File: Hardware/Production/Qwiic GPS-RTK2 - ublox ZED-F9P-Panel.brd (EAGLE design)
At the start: 43.2 x 43.2 mm, 125 parts, among them J1 Radio, J13 U.FL, J3 PTH, U2 3.3V, U3 ZED-F9P

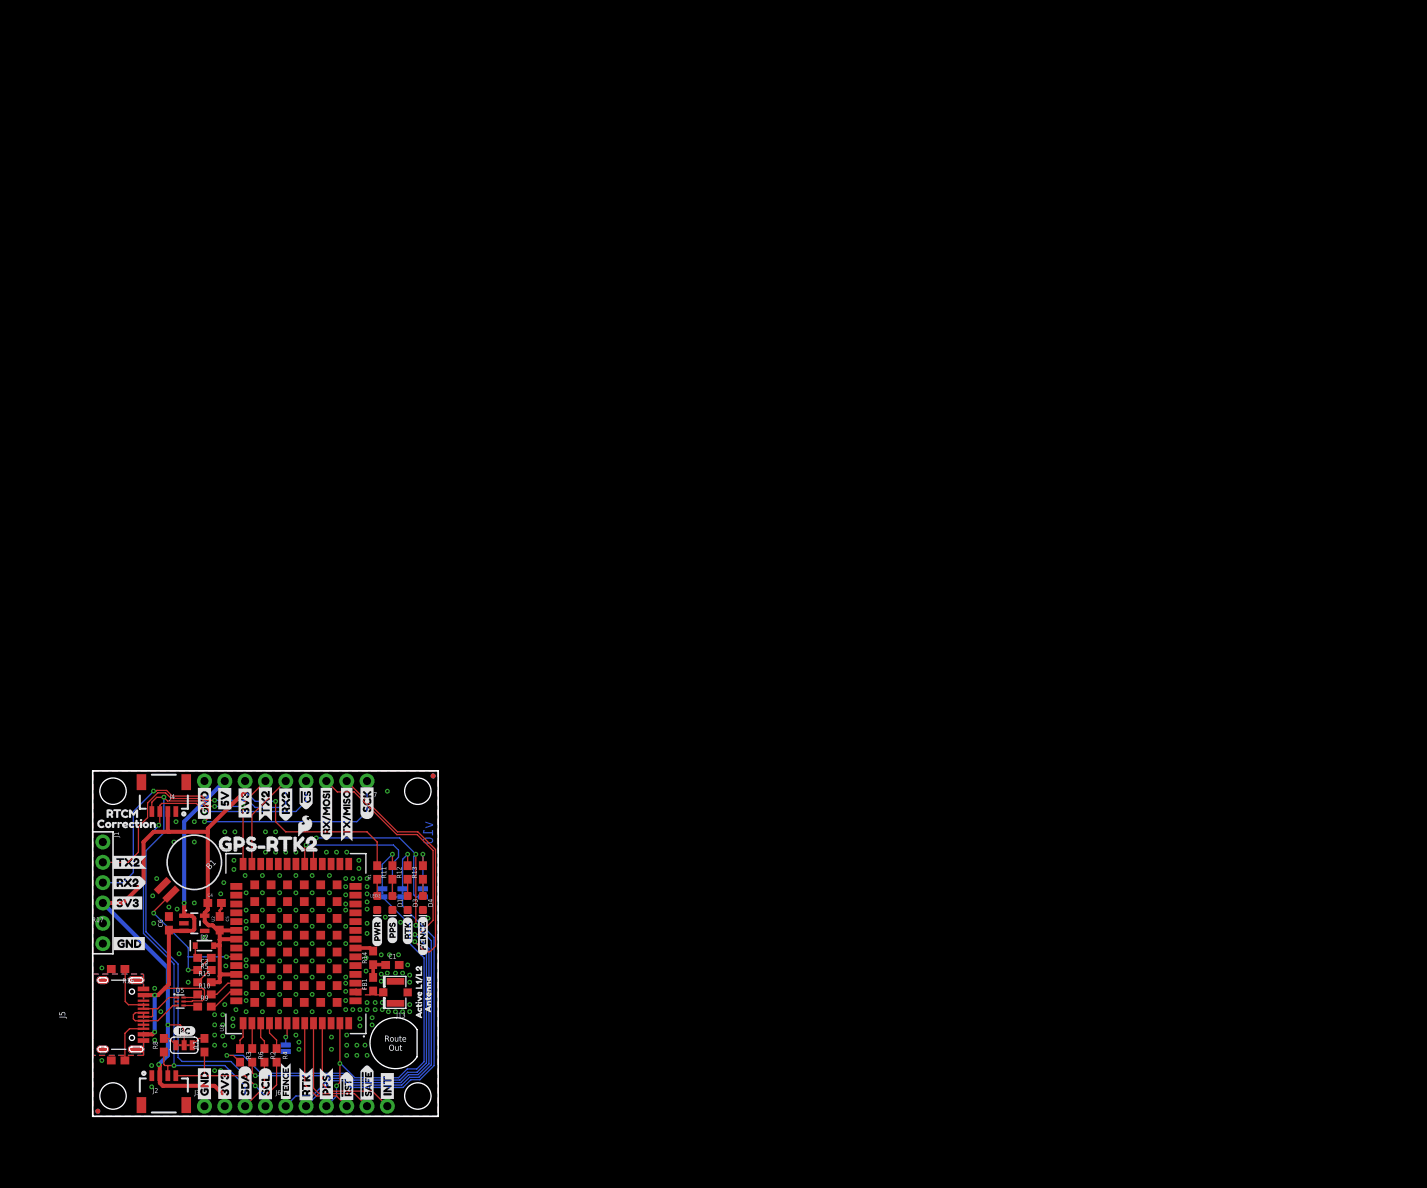
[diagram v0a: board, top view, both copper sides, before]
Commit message: v11 hardware: Added add' decoupling to USB VBUS, recomended induc to ant, more 33 ohm resistors.
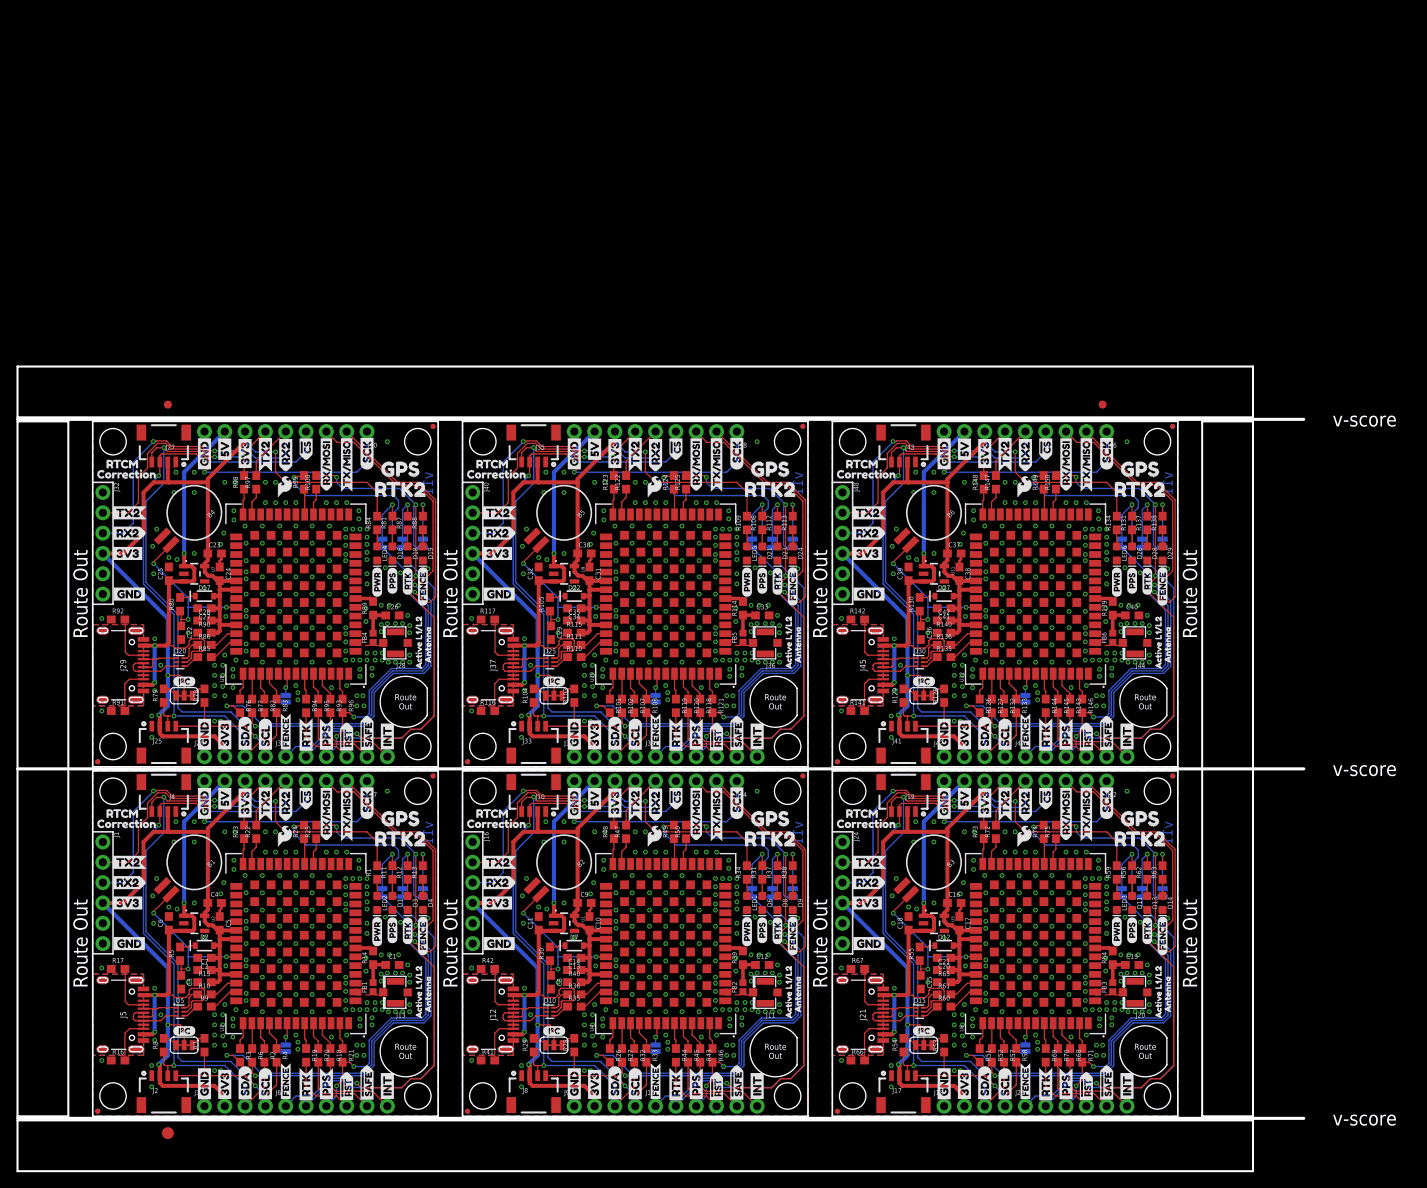
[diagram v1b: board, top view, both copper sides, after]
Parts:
- removed FRAME1: FRAME-LETTER, SparkFun-Aesthetics:CREATIVE_COMMONS
- added B2, B3, B4, B5, B6: 6.8MM_COIN_CELL, SparkFun-Batteries:BATTCON-6.8MM
- added C10, C14, C17, C21, C24, C28, C31, C35, C38, C42, C7: 0.1uF, SparkFun-Capacitors:0603
- added C11, C13, C15, C16, C18, C2, C20, C22, C23, C25, C27, C29, C30, C32, C34, C36, C37, C39, C41, C8, C9: 1.0uF, SparkFun-Capacitors:0603
- added C12, C19, C26, C33, C40: 47pF, SparkFun-Capacitors:0603
- added D10, D15, D20, D25, D30: PRTR5V0U2F, funbit:SOT886
- added D11, D16, D21, D26, D6: Yellow, SparkFun-LED:LED-0603
- added D12, D17, D22, D27, D7: 0.5A/40V/420mV, SparkFun-DiscreteSemi:SOD-323
- added D13, D18, D23, D28, D8: GREEN, SparkFun-LED:LED-0603
- added D14, D19, D24, D29, D9: BLUE, SparkFun-LED:LED-0603
- added E$1, E$2: (no value), SparkFun-Aesthetics:FIDUCIAL-1X2
- added E$3: (no value), SparkFun-Retired:FIDUCIAL-1.5X3
- added FB2, FB3, FB4, FB5, FB6: FERRITE_BEAD-120_OHM-0402, SparkFun-Coils:0402
- added J10, J17, J19, J25, J27, J33, J35, J41, J43, J8: (no value), SparkFun-Connectors:1X04_1MM_RA
- added J11, J20, J28, J36, J44: U.FL, SparkFun-Connectors:U.FL
- added J12, J21, J29, J37, J45: (no value), USB-C:USB-C-16P
- added J14, J22, J30, J38, J46: (no value), SparkFun-Connectors:1X09_NO_SILK
- added J15, J23, J31, J39, J47: (no value), SparkFun-Connectors:1X06_NO_SILK
- added J16, J24, J32, J40, J48: Radio, SparkFun-Connectors:1X06_NO_SILK
- added J18, J26, J34, J42, J9: PTH, SparkX:1X04_NO_SILK
- added JP10, JP24, JP38, JP52, JP66: (no value), SparkFun-Jumpers:SMT-JUMPER_3_2-NC_TRACE_SILK
- added JP11, JP17, JP18, JP25, JP32, JP33, JP39, JP46, JP47, JP53, JP59, JP60, JP67, JP74, JP75: (no value), SparkFun-Jumpers:SMT-JUMPER_2_NC_TRACE_SILK
- added JP12, JP13, JP22, JP23, JP26, JP27, JP36, JP37, JP40, JP42, JP50, JP51, JP54, JP55, JP64, JP65, JP68, JP69, JP8, JP9: FIDUCIALUFIDUCIAL, SparkFun:MICRO-FIDUCIAL
- added JP14, JP15, JP19, JP20, JP28, JP29, JP34, JP35, JP43, JP44, JP48, JP49, JP56, JP57, JP6, JP62, JP63, JP7, JP70, JP72: STAND-OFF, SparkFun:STAND-OFF
- added JP16, JP30, JP45, JP58, JP73: (no value), SparkFun-Jumpers:SMT-JUMPER_2_NO_SILK
- added LED1, LED3, LED4, LED5, LED6: RED, SparkFun-LED:LED-0603
- added LOGO10, LOGO12, LOGO4, LOGO6, LOGO8: SFE_LOGO_NAME_FLAME.1_INCH, SparkFun-Aesthetics:SFE_LOGO_NAME_FLAME_.1
- added LOGO11, LOGO3, LOGO5, LOGO7, LOGO9: OSHW-LOGOMINI, SparkFun-Aesthetics:OSHW-LOGO-MINI
- added R100, R101, R102, R107, R108, R118, R119, R120, R121, R122, R123, R124, R125, R126, R127, R132, R133, R143, R144, R145, R146, R147, R148, R149, R150, R18, R19, R20, R21, R22, R23, R24, R25, R26, R27, R32, R33, R43, R44, R45, R46, R47, R48, R49, R50, R51, R52, R57, R58, R68, R69, R70, R71, R72, R73, R74, R75, R76, R77, R82, R83, R93, R94, R95, R96, R97, R98, R99: 33, SparkFun-Resistors:0603
- added R103, R104, R128, R129, R28, R29, R53, R54, R78, R79: 2.2k, SparkFun-Resistors:0603
- added R105, R106, R109, R112, R113, R130, R131, R134, R137, R138, R30, R31, R34, R37, R38, R55, R56, R59, R62, R63, R80, R81, R84, R87, R88: 1k, SparkFun-Resistors:0603
- added R110, R111, R135, R136, R35, R36, R60, R61, R85, R86: 27, SparkFun-Resistors:0603
- added R114, R139, R39, R64, R89: 10, SparkFun-Resistors:0603
- added R115, R140, R40, R65, R90: 100k, SparkFun-Resistors:0603
- added R116, R117, R141, R142, R41, R42, R66, R67, R91, R92: 5.1k, SparkFun-Resistors:0603
- added U$100, U$145, U$146, U$168, U$169, U$214, U$215, U$237, U$238, U$283, U$284, U$306, U$307, U$352, U$353, U$375, U$376, U$76, U$77, U$99: (no value), Labels:GND-04
- added U$101, U$170, U$239, U$308, U$377: (no value), buzzard_labels (5):JP10
- added U$102, U$171, U$240, U$309, U$378: (no value), buzzard_labels (5):JP32
- added U$103, U$172, U$241, U$310, U$379: (no value), buzzard_labels (6):DSEL0
- added U$104, U$173, U$242, U$311, U$380: (no value), Labels:PWR-()-03
- added U$105, U$106, U$174, U$175, U$243, U$244, U$312, U$313, U$381, U$382: (no value), Labels:5V
- added U$107, U$108, U$176, U$177, U$245, U$246, U$314, U$315, U$383, U$384: (no value), Labels:CS#-<]
- added U$109, U$110, U$178, U$179, U$247, U$248, U$316, U$317, U$385, U$386: (no value), Labels:SCK-(]-04
- added U$111, U$180, U$249, U$318, U$387: (no value), SparkFun-Aesthetics:SFE_LOGO_FLAME_.1
- added U$112, U$124, U$181, U$193, U$250, U$262, U$319, U$331, U$388, U$400: (no value), buzzard_labels (36):RX#MOSI3
- added U$113, U$125, U$182, U$194, U$251, U$263, U$320, U$332, U$389, U$401: (no value), buzzard_labels (36):TX#MISO1
- added U$114, U$118, U$183, U$187, U$252, U$256, U$321, U$325, U$390, U$394: (no value), buzzard_labels (4):GND3
- added U$115, U$184, U$253, U$322, U$391: (no value), buzzard_labels (4):GPS#RTK28
- added U$116, U$117, U$143, U$144, U$166, U$167, U$185, U$186, U$212, U$213, U$235, U$236, U$254, U$255, U$281, U$282, U$304, U$305, U$323, U$324, U$350, U$351, U$373, U$374, U$392, U$393, U$74, U$75, U$97, U$98: (no value), Labels:3V3-04
- added U$119, U$123, U$188, U$192, U$257, U$261, U$326, U$330, U$395, U$399: (no value), buzzard_labels (4):CORRECTION0
- added U$120, U$122, U$189, U$191, U$258, U$260, U$327, U$329, U$396, U$398: (no value), buzzard_labels (4):RTCM5
- added U$121, U$190, U$259, U$328, U$397: (no value), buzzard_labels (4):ZED#F9P6
- added U$126, U$195, U$264, U$333, U$402: SMA-ANTENNA-THREADED, SparkFun-Hardware:SMA-THREADED
- added U$127, U$196, U$265, U$334, U$403: (no value), buzzard_labels (8):ACTIVE_L1#L21
- added U$128, U$197, U$266, U$335, U$404: (no value), buzzard_labels (8):ANTENNA2
- added U$129, U$134, U$136, U$198, U$203, U$205, U$267, U$272, U$274, U$336, U$341, U$343, U$405, U$410, U$412: (no value), buzzard_labels (10):RX20
- added U$130, U$199, U$268, U$337, U$406: (no value), buzzard_labels (10):RX22
- added U$131, U$133, U$135, U$200, U$202, U$204, U$269, U$271, U$273, U$338, U$340, U$342, U$407, U$409, U$411: (no value), buzzard_labels (10):TX21
- added U$132, U$201, U$270, U$339, U$408: (no value), buzzard_labels (10):TX23
- added U$137, U$206, U$275, U$344, U$413, U$59: (no value), buzzard_labels (4):GPS0
- added U$138, U$207, U$276, U$345, U$414, U$64: (no value), buzzard_labels (4):RTK21
- added U$139, U$141, U$208, U$210, U$277, U$279, U$346, U$348, U$72: (no value), Labels:SDA-[)
- added U$140, U$142, U$209, U$211, U$278, U$280, U$347, U$349, U$73: (no value), Labels:SCL-[)
- added U$147, U$216, U$285, U$354, U$78: (no value), Labels:I_SUPER2_C-()-03
- added U$148, U$149, U$217, U$218, U$286, U$287, U$355, U$356, U$79, U$80: (no value), buzzard_labels (5):INT8
- added U$150, U$219, U$288, U$357, U$81: (no value), buzzard_labels (5):U#BLOX3
- added U$151, U$220, U$289, U$358, U$82: (no value), Labels:QWIIC-LOGO-MEDIUM
- added U$152, U$153, U$221, U$222, U$290, U$291, U$359, U$360, U$83, U$84: (no value), buzzard_labels (7):#RST3
- added U$154, U$155, U$223, U$224, U$292, U$293, U$361, U$362, U$85, U$86: (no value), buzzard_labels (7):#SAFE1
- added U$156, U$157, U$225, U$226, U$294, U$295, U$363, U$364, U$87, U$88: (no value), buzzard_labels (7):PPS5
- added U$158, U$227, U$296, U$365, U$89: (no value), buzzard_labels (33):PPS0
- added U$159, U$228, U$297, U$366, U$90: (no value), buzzard_labels:FENCE2
- added U$160, U$229, U$298, U$367, U$91: (no value), buzzard_labels:JP20
- added U$161, U$230, U$299, U$368, U$92: (no value), buzzard_labels:RTK1
- added U$162, U$163, U$231, U$232, U$300, U$301, U$369, U$370, U$93, U$94: (no value), buzzard_labels (1):FENCE0
- added U$164, U$165, U$233, U$234, U$302, U$303, U$371, U$372, U$95, U$96: (no value), buzzard_labels (1):RTK1
- added U1, U11, U5, U7, U9: 3.3V, SparkFun-IC-Power:SOT23-5
- added U10, U12, U4, U6, U8: ZED-F9P, ZED-F9P:ZED-F9P
- FB1: value 30Ω/1.8A -> FERRITE_BEAD-120_OHM-0402; device SparkFun-Coils:0603 -> SparkFun-Coils:0402
- U$2: value SPECIAL_INSTRUCTIONS-ORDERING -> (none); device SparkFun-Aesthetics:ORDERING_INSTRUCTIONS -> Labels:SDA-[)
- U$47: device buzzard_labels (4):GPS#RTK29 -> Labels:SCL-[)
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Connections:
- new net !RESET1: J15.4, R44.2
- new net !RESET2: J23.4, R69.2
- new net !RESET3: J31.4, R94.2
- new net !RESET4: J39.4, R119.2
- new net !RESET5: J47.4, R144.2
- new net !SAFE1: J15.5, R45.2
- new net !SAFE2: J23.5, R70.2
- new net !SAFE3: J31.5, R95.2
- new net !SAFE4: J39.5, R120.2
- new net !SAFE5: J47.5, R145.2
- new net 3.3V1: C10.2, C13.1, C14.2, C9.1, D7.A, J10.2, J14.7, J16.4, J8.2, J9.2, JP10.2, R34.2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
- new net 3.3V2: C16.1, C17.2, C20.1, C21.2, D12.A, J17.2, J18.2, J19.2, J22.7, J24.4, JP24.2, R59.2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
- new net 3.3V3: C23.1, C24.2, C27.1, C28.2, D17.A, J25.2, J26.2, J27.2, J30.7, J32.4, JP38.2, R84.2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
- new net 3.3V4: C30.1, C31.2, C34.1, C35.2, D22.A, J33.2, J34.2, J35.2, J38.7, J40.4, JP52.2, R109.2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
- new net 3.3V5: C37.1, C38.2, C41.1, C42.2, D27.A, J41.2, J42.2, J43.2, J46.7, J48.4, JP66.2, R134.2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
- new net 5V1: C11.1, D10.5, J12.VBUS1, J12.VBUS2, J14.8, U1.1, U1.3
- new net 5V2: C18.1, D15.5, J21.VBUS1, J21.VBUS2, J22.8, U5.1, U5.3
- new net 5V3: C25.1, D20.5, J29.VBUS1, J29.VBUS2, J30.8, U7.1, U7.3
- new net 5V4: C32.1, D25.5, J37.VBUS1, J37.VBUS2, J38.8, U9.1, U9.3
- new net 5V5: C39.1, D30.5, J45.VBUS1, J45.VBUS2, J46.8, U11.1, U11.3
- new net ANT_VCC1: C12.1, FB2.2, R39.1
- new net ANT_VCC2: C19.1, FB3.2, R64.1
- new net ANT_VCC3: C26.1, FB4.2, R89.1
- new net ANT_VCC4: C33.1, FB5.2, R114.1
- new net ANT_VCC5: C40.1, FB6.2, R139.1
- new net BACKUP1: B2.+, C8.1, R30.1, U4.36
- new net BACKUP2: B3.+, C15.1, R55.1, U6.36
- new net BACKUP3: B4.+, C22.1, R80.1, U8.36
- new net BACKUP4: B5.+, C29.1, R105.1, U10.36
- new net BACKUP5: B6.+, C36.1, R130.1, U12.36
- new net CC10: J37.B5, R116.2
- new net CC11: J45.A5, R142.2
- new net CC12: J45.B5, R141.2
- new net CC3: J12.A5, R42.2
- new net CC4: J12.B5, R41.2
- new net CC5: J21.A5, R67.2
- new net CC6: J21.B5, R66.2
- new net CC7: J29.A5, R92.2
- new net CC8: J29.B5, R91.2
- new net CC9: J37.A5, R117.2
- new net D+1: D10.4, R35.1
- new net D+2: D15.4, R60.1
- new net D+3: D20.4, R85.1
- new net D+4: D25.4, R110.1
- new net D+5: D30.4, R135.1
- new net D-1: D10.6, R36.1
- new net D-2: D15.6, R61.1
- new net D-3: D20.6, R86.1
- new net D-4: D25.6, R111.1
- new net D-5: D30.6, R136.1
- new net D_SEL1: JP16.2, U4.47
- new net D_SEL2: JP30.2, U6.47
- new net D_SEL3: JP45.2, U8.47
- new net D_SEL4: JP58.2, U10.47
- new net D_SEL5: JP73.2, U12.47
- new net FENCE_STAT1: J15.1, JP18.2, R50.2
- new net FENCE_STAT2: J23.1, JP33.2, R75.2
- new net FENCE_STAT3: J31.1, JP47.2, R100.2
- new net FENCE_STAT4: J39.1, JP60.2, R125.2
- new net FENCE_STAT5: J47.1, JP75.2, R150.2
- new net GND1: B2.-, C10.1, C11.2, C12.2, C13.2, C14.1, C8.2, C9.2, D10.2, D6.C, D8.C, D9.C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
- new net GND2: B3.-, C15.2, C16.2, C17.1, C18.2, C19.2, C20.2, C21.1, D11.C, D13.C, D14.C, D15.2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
- new net GND3: B4.-, C22.2, C23.2, C24.1, C25.2, C26.2, C27.2, C28.1, D16.C, D18.C, D19.C, D20.2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
- new net GND4: B5.-, C29.2, C30.2, C31.1, C32.2, C33.2, C34.2, C35.1, D21.C, D23.C, D24.C, D25.2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
- new net GND5: B6.-, C36.2, C37.2, C38.1, C39.2, C40.2, C41.2, C42.1, D26.C, D28.C, D29.C, D30.2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
- new net GPS_ANT2: FB2.1, J11.FEED, U4.2
- new net GPS_ANT3: FB3.1, J20.FEED, U6.2
- new net GPS_ANT4: FB4.1, J28.FEED, U8.2
- new net GPS_ANT5: FB5.1, J36.FEED, U10.2
- new net GPS_ANT6: FB6.1, J44.FEED, U12.2
- new net INT1: J15.6, R43.2
- new net INT2: J23.6, R68.2
- new net INT3: J31.6, R93.2
- new net INT4: J39.6, R118.2
- new net INT5: J47.6, R143.2
- new net N$100: R125.1, U10.19
- new net N$101: JP66.1, R129.2
- new net N$102: JP66.3, R128.2
- new net N$103: D26.A, R131.1
- new net N$104: JP67.1, R131.2
- new net N$105: D27.C, R130.2
- new net N$106: LED6.A, R134.1
- new net N$107: R135.2, U12.40
- new net N$108: R136.2, U12.39
- new net N$109: D28.A, R137.1
- new net N$110: JP74.1, R137.2
- new net N$111: D29.A, R138.1
- new net N$112: JP75.1, R138.2
- new net N$113: R139.2, U12.7
- new net N$114: R147.1, U12.26
- new net N$115: R143.1, U12.51
- new net N$116: R144.1, U12.49
- new net N$117: R146.1, U12.53
- new net N$118: R145.1, U12.50
- new net N$119: R149.1, U12.20
- new net N$120: R150.1, U12.19
- new net N$14: R22.1, U3.26
- new net N$15: R18.1, U3.51
- new net N$16: R19.1, U3.49
- new net N$17: R21.1, U3.53
- new net N$18: R20.1, U3.50
- new net N$19: R24.1, U3.20
- new net N$20: R25.1, U3.19
- new net N$21: JP10.1, R29.2
- new net N$22: JP10.3, R28.2
- new net N$23: D6.A, R31.1
- new net N$24: JP11.1, R31.2
- new net N$25: D7.C, R30.2
- new net N$26: LED1.A, R34.1
- new net N$27: R35.2, U4.40
- new net N$28: R36.2, U4.39
- new net N$29: D8.A, R37.1
- new net N$30: JP17.1, R37.2
- new net N$31: D9.A, R38.1
- new net N$32: JP18.1, R38.2
- new net N$33: R39.2, U4.7
- new net N$34: R47.1, U4.26
- new net N$35: R43.1, U4.51
- new net N$36: R44.1, U4.49
- new net N$37: R46.1, U4.53
- new net N$38: R45.1, U4.50
- new net N$39: R49.1, U4.20
- new net N$40: R50.1, U4.19
- new net N$41: JP24.1, R54.2
- new net N$42: JP24.3, R53.2
- new net N$43: D11.A, R56.1
- new net N$44: JP25.1, R56.2
- new net N$45: D12.C, R55.2
- new net N$46: LED3.A, R59.1
- new net N$47: R60.2, U6.40
- new net N$48: R61.2, U6.39
- new net N$49: D13.A, R62.1
- new net N$50: JP32.1, R62.2
- new net N$51: D14.A, R63.1
- new net N$52: JP33.1, R63.2
- new net N$53: R64.2, U6.7
- new net N$54: R72.1, U6.26
- new net N$55: R68.1, U6.51
- new net N$56: R69.1, U6.49
- new net N$57: R71.1, U6.53
- new net N$58: R70.1, U6.50
- new net N$59: R74.1, U6.20
- new net N$60: R75.1, U6.19
- new net N$61: JP38.1, R79.2
- new net N$62: JP38.3, R78.2
- new net N$63: D16.A, R81.1
- new net N$64: JP39.1, R81.2
- new net N$65: D17.C, R80.2
- new net N$66: LED4.A, R84.1
- new net N$67: R85.2, U8.40
- new net N$68: R86.2, U8.39
- new net N$69: D18.A, R87.1
- new net N$70: JP46.1, R87.2
- new net N$71: D19.A, R88.1
- new net N$72: JP47.1, R88.2
- new net N$73: R89.2, U8.7
- new net N$74: R97.1, U8.26
- new net N$75: R93.1, U8.51
- new net N$76: R94.1, U8.49
- new net N$77: R96.1, U8.53
- new net N$78: R95.1, U8.50
- new net N$79: R99.1, U8.20
- new net N$80: R100.1, U8.19
- new net N$81: JP52.1, R104.2
- new net N$82: JP52.3, R103.2
- new net N$83: D21.A, R106.1
- new net N$84: JP53.1, R106.2
- new net N$85: D22.C, R105.2
- new net N$86: LED5.A, R109.1
- new net N$87: R110.2, U10.40
- new net N$88: R111.2, U10.39
- new net N$89: D23.A, R112.1
- new net N$90: JP59.1, R112.2
- new net N$91: D24.A, R113.1
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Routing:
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- added copper zone on layer 1, net GND1
- added copper zone on layer 16, net GND1
- added copper zone on layer 1, net GND2
- added copper zone on layer 16, net GND2
- added copper zone on layer 1, net GND3
- added copper zone on layer 16, net GND3
- added copper zone on layer 1, net GND4
- added copper zone on layer 16, net GND4
- added copper zone on layer 1, net GND5
- added copper zone on layer 16, net GND5
- added copper zone on layer 1, net GPS_ANT2
- added copper zone on layer 1, net GPS_ANT3
- added copper zone on layer 1, net GPS_ANT4
- added copper zone on layer 1, net GPS_ANT5
- added copper zone on layer 1, net GPS_ANT6
- added copper zone on layer 1, net SHLD1
- added copper zone on layer 16, net SHLD1
- added copper zone on layer 1, net SHLD2
- added copper zone on layer 16, net SHLD2
- added copper zone on layer 1, net SHLD3
- added copper zone on layer 16, net SHLD3
- added copper zone on layer 1, net SHLD4
- added copper zone on layer 16, net SHLD4
- added copper zone on layer 1, net SHLD5
- added copper zone on layer 16, net SHLD5
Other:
- board size 43.2 x 43.2 mm -> 160.8 x 100.6 mm
- board text added: "Route Out"
- board text added: "v-score"
- board text added: "v11"
- board text removed: "Board thickness is 0.8mm"
- board text removed: "Measurements in inches"
- board text removed: "No clean process"
- board text removed: "v10"

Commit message: Adding SMA connector to Antenna and SMA
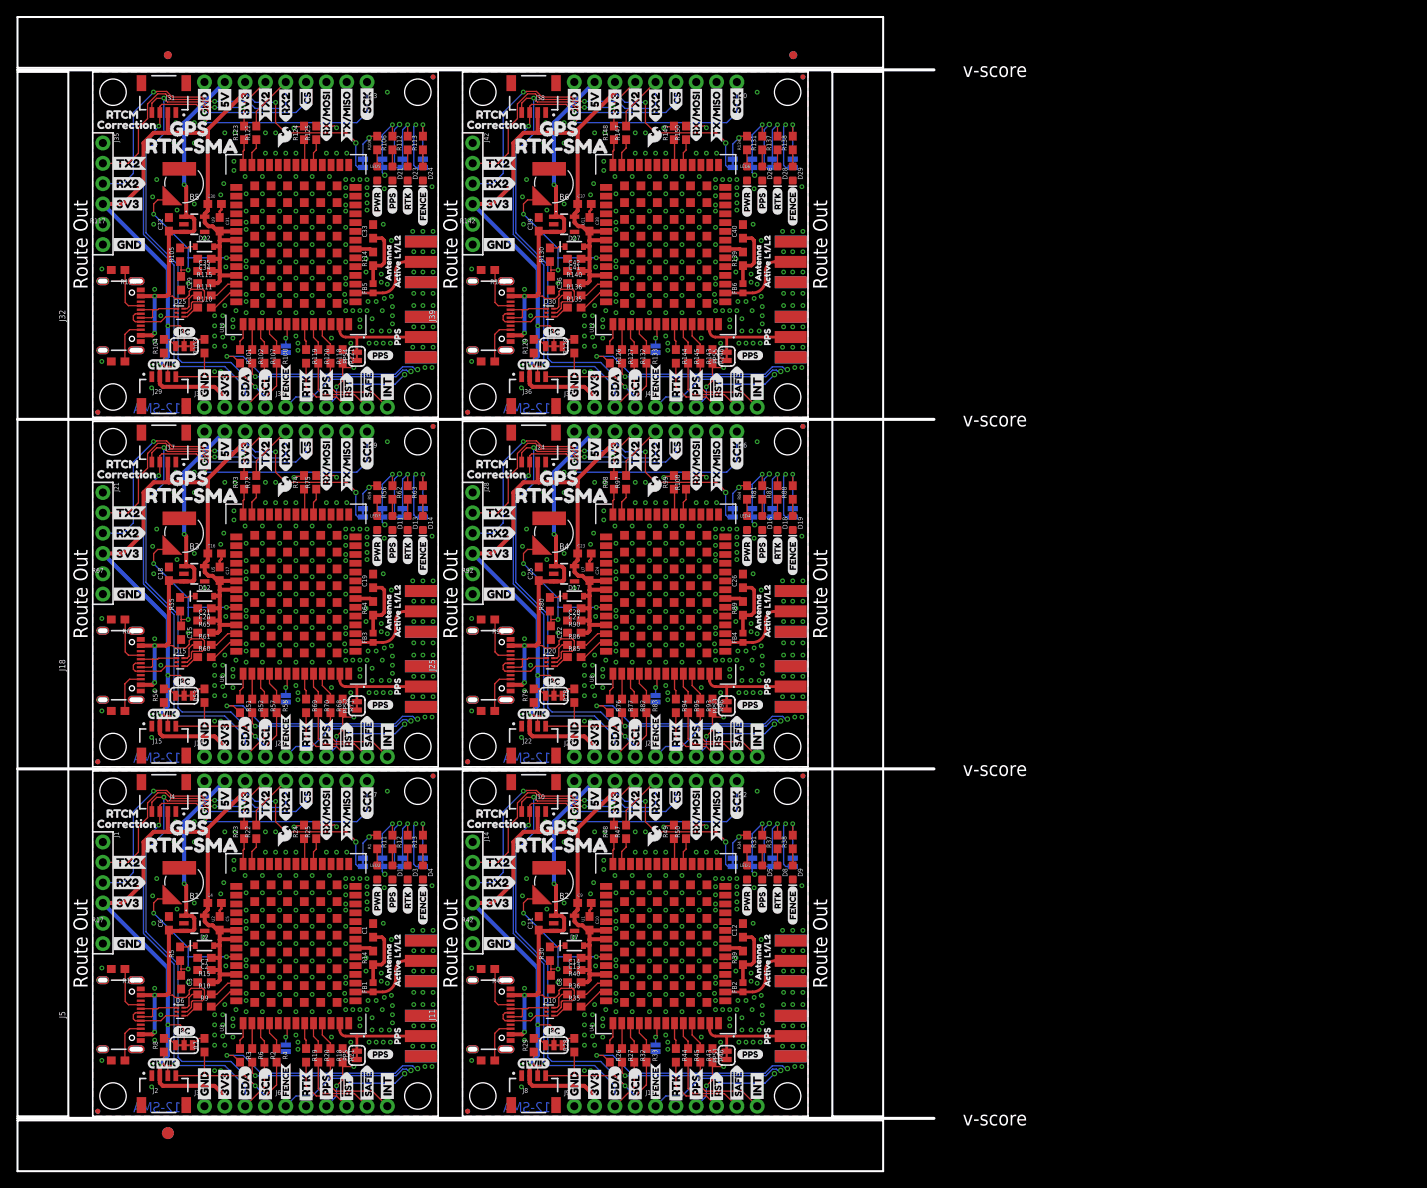
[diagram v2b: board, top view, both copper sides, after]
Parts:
- removed J43: (no value), SparkFun-Connectors:1X04_1MM_RA
- removed J44: U.FL, SparkFun-Connectors:U.FL
- removed J45: (no value), USB-C:USB-C-16P
- removed J46: (no value), SparkFun-Connectors:1X09_NO_SILK
- removed J47: (no value), SparkFun-Connectors:1X06_NO_SILK
- removed J48: Radio, SparkFun-Connectors:1X06_NO_SILK
- removed JP50, JP51, JP54, JP55, JP64, JP65, JP68, JP69: FIDUCIALUFIDUCIAL, SparkFun:MICRO-FIDUCIAL
- removed JP52, JP66: (no value), SparkFun-Jumpers:SMT-JUMPER_3_2-NC_TRACE_SILK
- removed JP53, JP59, JP60, JP67, JP74, JP75: (no value), SparkFun-Jumpers:SMT-JUMPER_2_NC_TRACE_SILK
- removed JP56, JP57, JP62, JP63, JP70, JP72: STAND-OFF, SparkFun:STAND-OFF
- removed JP73: (no value), SparkFun-Jumpers:SMT-JUMPER_2_NO_SILK
- added E$4: (no value), SparkFun-Aesthetics:FIDUCIAL-1X2
- added E$5, E$6: (no value), SparkFun-Retired:FIDUCIAL-1.5X3
- added E1, E10, E11, E12, E2, E3, E4, E5, E6, E7, E8, E9: SMA, SparkFun-RF:SMA-EDGE
- added FENCE, FENCE1, FENCE2, FENCE3, FENCE4, FENCE5, PPS, PPS1, PPS2, PPS3, PPS4, PPS5, PPS_LED, PPS_LED1, PPS_LED2, PPS_LED3, PPS_LED4, PPS_LED5, PWR, PWR1, PWR2, PWR3, PWR4, PWR5, RTK, RTK1, RTK2, RTK3, RTK4, RTK5: (no value), SparkFun-Jumpers:SMT-JUMPER_2_NC_TRACE_SILK
- added SPI, SPI1, SPI2, SPI4, SPI5: (no value), SparkFun-Jumpers:SMT-JUMPER_2_NO_SILK
- added U$415: (no value), buzzard_labels (36):RX#MOSI3
- added U$416: (no value), buzzard_labels (36):TX#MISO1
- added U$417: (no value), buzzard_labels (8):ACTIVE_L1#L21
- added U$418, U$437: (no value), buzzard_labels (8):ANTENNA2
- added U$419, U$424, U$426: (no value), buzzard_labels (10):RX20
- added U$420: (no value), buzzard_labels (10):RX22
- added U$421, U$423, U$425: (no value), buzzard_labels (10):TX21
- added U$422: (no value), buzzard_labels (10):TX23
- added U$427: (no value), buzzard_labels (4):GPS0
- added U$428: (no value), SparkFun-Aesthetics:QWIIC_4MM
- added U$429, U$436: (no value), buzzard_labels (2):PPS1
- added U$430: (no value), Labels:PWR-()-03
- added U$431, U$434: (no value), buzzard_labels (33):PPS0
- added U$432: (no value), buzzard_labels:RTK1
- added U$433: (no value), buzzard_labels:FENCE2
- added U$435: (no value), buzzard_labels (3):RTK#SMA4
- added U$438: (no value), buzzard_labels (4):GPS#RTK#SMA5
- B1, B2, B3, B4, B5, B6: device SparkFun-Batteries:BATTCON-6.8MM -> SparkFun-Batteries:ML414H_IV01E
- D10, D15, D20, D25, D30: device funbit:SOT886 -> SparkFun-IC-Power:SOT886
- D5: value PRTR5V0U2F -> Yellow; device funbit:SOT886 -> SparkFun-LED:LED-0603
- D6: value Yellow -> PRTR5V0U2F; device SparkFun-LED:LED-0603 -> SparkFun-IC-Power:SOT886
- E$3: device SparkFun-Retired:FIDUCIAL-1.5X3 -> SparkFun-Aesthetics:FIDUCIAL-1X2
- FB1, FB2, FB3, FB4, FB5, FB6: value FERRITE_BEAD-120_OHM-0402 -> 120_OHM
- J10, J17, J2, J4, J8: value (none) -> Qwiic Right Angle; device SparkFun-Connectors:1X04_1MM_RA -> SparkFun-Connectors:JST04_1MM_RA
- J11: value U.FL -> (none); device SparkFun-Connectors:U.FL -> SparkFun-Connectors:USB-C-16P-2LAYER-PADS
- J12: device USB-C:USB-C-16P -> SparkFun-Connectors:1X09_NO_SILK
- J13, J20: value U.FL -> (none); device SparkFun-Connectors:U.FL -> SparkFun-Connectors:1X06_NO_SILK
- J14: value (none) -> Radio; device SparkFun-Connectors:1X09_NO_SILK -> SparkFun-Connectors:1X06_NO_SILK
- J15, J31: value (none) -> Qwiic Right Angle; device SparkFun-Connectors:1X06_NO_SILK -> SparkFun-Connectors:JST04_1MM_RA
- J16: value Radio -> PTH; device SparkFun-Connectors:1X06_NO_SILK -> SparkX:1X04_NO_SILK
- J18: value PTH -> (none); device SparkX:1X04_NO_SILK -> SparkFun-Connectors:USB-C-16P-2LAYER-PADS
- J19, J33: device SparkFun-Connectors:1X04_1MM_RA -> SparkFun-Connectors:1X09_NO_SILK
- J21: value (none) -> Radio; device USB-C:USB-C-16P -> SparkFun-Connectors:1X06_NO_SILK
- J22, J38: value (none) -> Qwiic Right Angle; device SparkFun-Connectors:1X09_NO_SILK -> SparkFun-Connectors:JST04_1MM_RA
- J23: value (none) -> PTH; device SparkFun-Connectors:1X06_NO_SILK -> SparkX:1X04_NO_SILK
- J24: value Radio -> Qwiic Right Angle; device SparkFun-Connectors:1X06_NO_SILK -> SparkFun-Connectors:JST04_1MM_RA
- J25: device SparkFun-Connectors:1X04_1MM_RA -> SparkFun-Connectors:USB-C-16P-2LAYER-PADS
- J26: value PTH -> (none); device SparkX:1X04_NO_SILK -> SparkFun-Connectors:1X09_NO_SILK
- J27, J41: device SparkFun-Connectors:1X04_1MM_RA -> SparkFun-Connectors:1X06_NO_SILK
- J28: value U.FL -> Radio; device SparkFun-Connectors:U.FL -> SparkFun-Connectors:1X06_NO_SILK
- J29: value (none) -> Qwiic Right Angle; device USB-C:USB-C-16P -> SparkFun-Connectors:JST04_1MM_RA
- J30: value (none) -> PTH; device SparkFun-Connectors:1X09_NO_SILK -> SparkX:1X04_NO_SILK
- J32: value Radio -> (none); device SparkFun-Connectors:1X06_NO_SILK -> SparkFun-Connectors:USB-C-16P-2LAYER-PADS
- J34: value PTH -> (none); device SparkX:1X04_NO_SILK -> SparkFun-Connectors:1X06_NO_SILK
- J35: value (none) -> Radio; device SparkFun-Connectors:1X04_1MM_RA -> SparkFun-Connectors:1X06_NO_SILK
- J36: value U.FL -> Qwiic Right Angle; device SparkFun-Connectors:U.FL -> SparkFun-Connectors:JST04_1MM_RA
- J37: value (none) -> PTH; device USB-C:USB-C-16P -> SparkX:1X04_NO_SILK
- J39: device SparkFun-Connectors:1X06_NO_SILK -> SparkFun-Connectors:USB-C-16P-2LAYER-PADS
- J40: value Radio -> (none); device SparkFun-Connectors:1X06_NO_SILK -> SparkFun-Connectors:1X09_NO_SILK
- J42: value PTH -> Radio; device SparkX:1X04_NO_SILK -> SparkFun-Connectors:1X06_NO_SILK
- J5: device USB-C:USB-C-16P -> SparkFun-Connectors:USB-C-16P-2LAYER-PADS
- JP1, JP11, JP18, JP2, JP32, JP39: value (none) -> STAND-OFF; device SparkFun-Jumpers:SMT-JUMPER_2_NC_TRACE_SILK -> SparkFun:STAND-OFF
- JP10, JP38: value (none) -> STAND-OFF; device SparkFun-Jumpers:SMT-JUMPER_3_2-NC_TRACE_SILK -> SparkFun:STAND-OFF
- JP12, JP22, JP40, JP42, JP9: value FIDUCIALUFIDUCIAL -> STAND-OFF; device SparkFun:MICRO-FIDUCIAL -> SparkFun:STAND-OFF
- JP14, JP34, JP43, JP44, JP7: value STAND-OFF -> FIDUCIALUFIDUCIAL; device SparkFun:STAND-OFF -> SparkFun:MICRO-FIDUCIAL
- JP15, JP35, JP6: value STAND-OFF -> (none); device SparkFun:STAND-OFF -> SparkFun-Jumpers:SMT-JUMPER_3_2-NC_TRACE_SILK
- JP16, JP4: value (none) -> FIDUCIALUFIDUCIAL; device SparkFun-Jumpers:SMT-JUMPER_2_NO_SILK -> SparkFun:MICRO-FIDUCIAL
- JP17, JP3, JP33, JP46, JP47: value (none) -> FIDUCIALUFIDUCIAL; device SparkFun-Jumpers:SMT-JUMPER_2_NC_TRACE_SILK -> SparkFun:MICRO-FIDUCIAL
- JP24: value (none) -> FIDUCIALUFIDUCIAL; device SparkFun-Jumpers:SMT-JUMPER_3_2-NC_TRACE_SILK -> SparkFun:MICRO-FIDUCIAL
- JP25: device SparkFun-Jumpers:SMT-JUMPER_2_NC_TRACE_SILK -> SparkFun-Jumpers:SMT-JUMPER_3_2-NC_TRACE_SILK
- JP30: value (none) -> STAND-OFF; device SparkFun-Jumpers:SMT-JUMPER_2_NO_SILK -> SparkFun:STAND-OFF
- JP45: device SparkFun-Jumpers:SMT-JUMPER_2_NO_SILK -> SparkFun-Jumpers:SMT-JUMPER_3_2-NC_TRACE_SILK
- U$100, U$99: device Labels:GND-04 -> Labels:3V3-04
- U$101: device buzzard_labels (5):JP10 -> Labels:GND-04
- U$102: device buzzard_labels (5):JP32 -> Labels:GND-04
- U$115, U$391: device buzzard_labels (4):GPS#RTK28 -> Labels:3V3-04
- U$117: device Labels:3V3-04 -> buzzard_labels (4):GND3
- U$118: device buzzard_labels (4):GND3 -> buzzard_labels (4):CORRECTION0
- U$119, U$192: device buzzard_labels (4):CORRECTION0 -> buzzard_labels (4):RTCM5
- U$12: device buzzard_labels:JP20 -> Labels:PWR-()-03
- U$120: device buzzard_labels (4):RTCM5 -> buzzard_labels (4):ZED#F9P6
- U$121: device buzzard_labels (4):ZED#F9P6 -> buzzard_labels (4):RTCM5
- U$122, U$191: device buzzard_labels (4):RTCM5 -> buzzard_labels (4):CORRECTION0
- U$123: device buzzard_labels (4):CORRECTION0 -> buzzard_labels (36):RX#MOSI3
- U$124: device buzzard_labels (36):RX#MOSI3 -> buzzard_labels (36):TX#MISO1
- U$125: device buzzard_labels (36):TX#MISO1 -> buzzard_labels (8):ACTIVE_L1#L21
- U$126: value SMA-ANTENNA-THREADED -> (none); device SparkFun-Hardware:SMA-THREADED -> buzzard_labels (8):ANTENNA2
- U$127: device buzzard_labels (8):ACTIVE_L1#L21 -> buzzard_labels (10):RX20
- U$128: device buzzard_labels (8):ANTENNA2 -> buzzard_labels (10):RX22
- U$129: device buzzard_labels (10):RX20 -> buzzard_labels (10):TX21
- U$130: device buzzard_labels (10):RX22 -> buzzard_labels (10):TX23
- U$132: device buzzard_labels (10):TX23 -> buzzard_labels (10):RX20
- U$135: device buzzard_labels (10):TX21 -> buzzard_labels (4):GPS0
- U$136: device buzzard_labels (10):RX20 -> SparkFun-Aesthetics:QWIIC_4MM
- U$137: device buzzard_labels (4):GPS0 -> buzzard_labels (2):PPS1
- U$138: device buzzard_labels (4):RTK21 -> Labels:PWR-()-03
- U$139, U$72: device Labels:SDA-[) -> buzzard_labels (33):PPS0
- U$140: device Labels:SCL-[) -> buzzard_labels:RTK1
- U$141: device Labels:SDA-[) -> buzzard_labels:FENCE2
- U$142: device Labels:SCL-[) -> buzzard_labels (33):PPS0
- U$143: device Labels:3V3-04 -> buzzard_labels (3):RTK#SMA4
- U$144, U$74: device Labels:3V3-04 -> buzzard_labels (2):PPS1
- U$145: device Labels:GND-04 -> buzzard_labels (8):ANTENNA2
- U$146, U$76: device Labels:GND-04 -> buzzard_labels (4):GPS#RTK#SMA5
- U$147: device Labels:I_SUPER2_C-()-03 -> Labels:SDA-[)
- U$148: device buzzard_labels (5):INT8 -> Labels:SCL-[)
- U$149: device buzzard_labels (5):INT8 -> Labels:SDA-[)
- U$150: device buzzard_labels (5):U#BLOX3 -> Labels:SCL-[)
- U$151: device Labels:QWIIC-LOGO-MEDIUM -> Labels:3V3-04
- U$152: device buzzard_labels (7):#RST3 -> Labels:3V3-04
- U$153: device buzzard_labels (7):#RST3 -> Labels:GND-04
- U$154: device buzzard_labels (7):#SAFE1 -> Labels:GND-04
- U$155: device buzzard_labels (7):#SAFE1 -> Labels:I_SUPER2_C-()-03
- U$156, U$157: device buzzard_labels (7):PPS5 -> buzzard_labels (5):INT8
- U$158: device buzzard_labels (33):PPS0 -> buzzard_labels (5):U#BLOX3
- U$159: device buzzard_labels:FENCE2 -> buzzard_labels (7):#RST3
- U$160: device buzzard_labels:JP20 -> buzzard_labels (7):#RST3
- U$161: device buzzard_labels:RTK1 -> buzzard_labels (7):#SAFE1
- U$162: device buzzard_labels (1):FENCE0 -> buzzard_labels (7):#SAFE1
- U$163: device buzzard_labels (1):FENCE0 -> buzzard_labels (7):PPS5
- U$164: device buzzard_labels (1):RTK1 -> buzzard_labels (7):PPS5
- U$165: device buzzard_labels (1):RTK1 -> buzzard_labels (33):PPS0
- U$166: device Labels:3V3-04 -> buzzard_labels:FENCE2
- U$167, U$213: device Labels:3V3-04 -> buzzard_labels:RTK1
- U$168, U$169: device Labels:GND-04 -> buzzard_labels (1):FENCE0
- U$170: device buzzard_labels (5):JP10 -> buzzard_labels (1):RTK1
- U$171: device buzzard_labels (5):JP32 -> buzzard_labels (1):RTK1
- U$172: device buzzard_labels (6):DSEL0 -> Labels:3V3-04
- U$173: device Labels:PWR-()-03 -> Labels:3V3-04
- U$174, U$175: device Labels:5V -> Labels:GND-04
- U$176: device Labels:CS#-<] -> buzzard_labels (6):DSEL0
- U$177: device Labels:CS#-<] -> Labels:PWR-()-03
- U$178, U$179: device Labels:SCK-(]-04 -> Labels:5V
- U$180: device SparkFun-Aesthetics:SFE_LOGO_FLAME_.1 -> Labels:CS#-<]
- U$181, U$400: device buzzard_labels (36):RX#MOSI3 -> Labels:CS#-<]
- U$182, U$401: device buzzard_labels (36):TX#MISO1 -> Labels:SCK-(]-04
- U$183, U$256: device buzzard_labels (4):GND3 -> Labels:SCK-(]-04
- U$184: device buzzard_labels (4):GPS#RTK28 -> SparkFun-Aesthetics:SFE_LOGO_FLAME_.1
- U$185: device Labels:3V3-04 -> buzzard_labels (36):RX#MOSI3
- U$186: device Labels:3V3-04 -> buzzard_labels (36):TX#MISO1
- U$188, U$261: device buzzard_labels (4):CORRECTION0 -> Labels:3V3-04
- U$189: device buzzard_labels (4):RTCM5 -> Labels:3V3-04
- U$190: device buzzard_labels (4):ZED#F9P6 -> buzzard_labels (4):GND3
- U$193: device buzzard_labels (36):RX#MOSI3 -> buzzard_labels (4):ZED#F9P6
- U$194: device buzzard_labels (36):TX#MISO1 -> buzzard_labels (4):RTCM5
- U$195, U$264: value SMA-ANTENNA-THREADED -> (none); device SparkFun-Hardware:SMA-THREADED -> buzzard_labels (4):CORRECTION0
- U$196: device buzzard_labels (8):ACTIVE_L1#L21 -> buzzard_labels (36):RX#MOSI3
- U$197: device buzzard_labels (8):ANTENNA2 -> buzzard_labels (36):TX#MISO1
- U$198: device buzzard_labels (10):RX20 -> buzzard_labels (8):ACTIVE_L1#L21
- U$199: device buzzard_labels (10):RX22 -> buzzard_labels (8):ANTENNA2
- U$200, U$273: device buzzard_labels (10):TX21 -> buzzard_labels (10):RX20
- U$201: device buzzard_labels (10):TX23 -> buzzard_labels (10):RX22
- U$203: device buzzard_labels (10):RX20 -> buzzard_labels (10):TX23
- U$206, U$275: device buzzard_labels (4):GPS0 -> buzzard_labels (10):TX21
- U$207: device buzzard_labels (4):RTK21 -> buzzard_labels (10):RX20
- U$208: device Labels:SDA-[) -> buzzard_labels (4):GPS0
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- renumbered JP58 to SPI3
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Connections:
- removed net N$101 (its old number): JP66.1, R129.2
- removed net N$102 (its old number): JP66.3, R128.2
- removed net N$110 (its old number): JP74.1, R137.2
- removed net N$112 (its old number): JP75.1, R138.2
- removed net N$30 (its old number): JP17.1, R37.2
- removed net N$32 (its old number): JP18.1, R38.2
- removed net N$37 (its old number): R46.1, U4.53
- removed net N$50 (its old number): JP32.1, R62.2
- removed net N$57 (its old number): R71.1, U6.53
- removed net N$61 (its old number): JP38.1, R79.2
- removed net N$70 (its old number): JP46.1, R87.2
- removed net N$72 (its old number): JP47.1, R88.2
- removed net N$77 (its old number): R96.1, U8.53
- removed net N$81 (its old number): JP52.1, R104.2
- removed net N$82 (its old number): JP52.3, R103.2
- removed net N$90 (its old number): JP59.1, R112.2
- removed net N$92 (its old number): JP60.1, R113.2
- removed net N$97 (its old number): R121.1, U10.53
- removed net SHLD: J5.SHLD1, J5.SHLD2, J5.SHLD3, J5.SHLD4, J5.SHLD5, J5.SHLD6, J5.SHLD7, J5.SHLD8
- removed net SHLD1: J12.SHLD1, J12.SHLD2, J12.SHLD3, J12.SHLD4, J12.SHLD5, J12.SHLD6, J12.SHLD7, J12.SHLD8
- removed net SHLD2: J21.SHLD1, J21.SHLD2, J21.SHLD3, J21.SHLD4, J21.SHLD5, J21.SHLD6, J21.SHLD7, J21.SHLD8
- removed net SHLD3: J29.SHLD1, J29.SHLD2, J29.SHLD3, J29.SHLD4, J29.SHLD5, J29.SHLD6, J29.SHLD7, J29.SHLD8
- removed net SHLD4: J37.SHLD1, J37.SHLD2, J37.SHLD3, J37.SHLD4, J37.SHLD5, J37.SHLD6, J37.SHLD7, J37.SHLD8
- removed net SHLD5: J45.SHLD1, J45.SHLD2, J45.SHLD3, J45.SHLD4, J45.SHLD5, J45.SHLD6, J45.SHLD7, J45.SHLD8
- new net N$105: PWR4.1, R109.2
- new net N$106: JP45.1, R129.2
- new net N$107: JP45.3, R128.2
- new net N$109: PPS_LED5.1, R131.2
- new net N$115: R137.2, RTK5.1
- new net N$125: PPS5.1, R146.1
- new net N$126: PWR5.1, R134.2
- new net N$25: PPS_LED1.1, R31.2
- new net N$31: R37.2, RTK1.1
- new net N$33: FENCE1.1, R38.2
- new net N$43: JP15.1, R54.2
- new net N$46: PPS_LED2.1, R56.2
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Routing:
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- added copper zone on layer 15, net GND
- added copper zone on layer 2, net GND
- added copper zone on layer 15, net GND1
- added copper zone on layer 2, net GND1
- added copper zone on layer 15, net GND2
- added copper zone on layer 2, net GND2
- added copper zone on layer 15, net GND3
- added copper zone on layer 2, net GND3
- added copper zone on layer 15, net GND4
- added copper zone on layer 2, net GND4
- added copper zone on layer 15, net GND5
- added copper zone on layer 2, net GND5
- removed copper zone on layer 1, net GPS_ANT1
- removed copper zone on layer 1, net GPS_ANT2
- removed copper zone on layer 1, net GPS_ANT3
- removed copper zone on layer 1, net GPS_ANT4
- removed copper zone on layer 1, net GPS_ANT5
- removed copper zone on layer 1, net GPS_ANT6
- removed copper zone on layer 1, net SHLD
- removed copper zone on layer 16, net SHLD
- removed copper zone on layer 1, net SHLD1
- removed copper zone on layer 16, net SHLD1
- removed copper zone on layer 1, net SHLD2
- removed copper zone on layer 16, net SHLD2
- removed copper zone on layer 1, net SHLD3
- removed copper zone on layer 16, net SHLD3
- removed copper zone on layer 1, net SHLD4
- removed copper zone on layer 16, net SHLD4
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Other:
- board size 160.8 x 100.6 mm -> 114.6 x 144.3 mm
- board text added: "v12-SMA"
- board text removed: "v11"
